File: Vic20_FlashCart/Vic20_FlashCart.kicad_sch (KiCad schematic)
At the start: 45 parts, among them U1 SST39LF040, U2 SST39LF040, U3 IS62C256AL, U4 7400, U5 74LS21

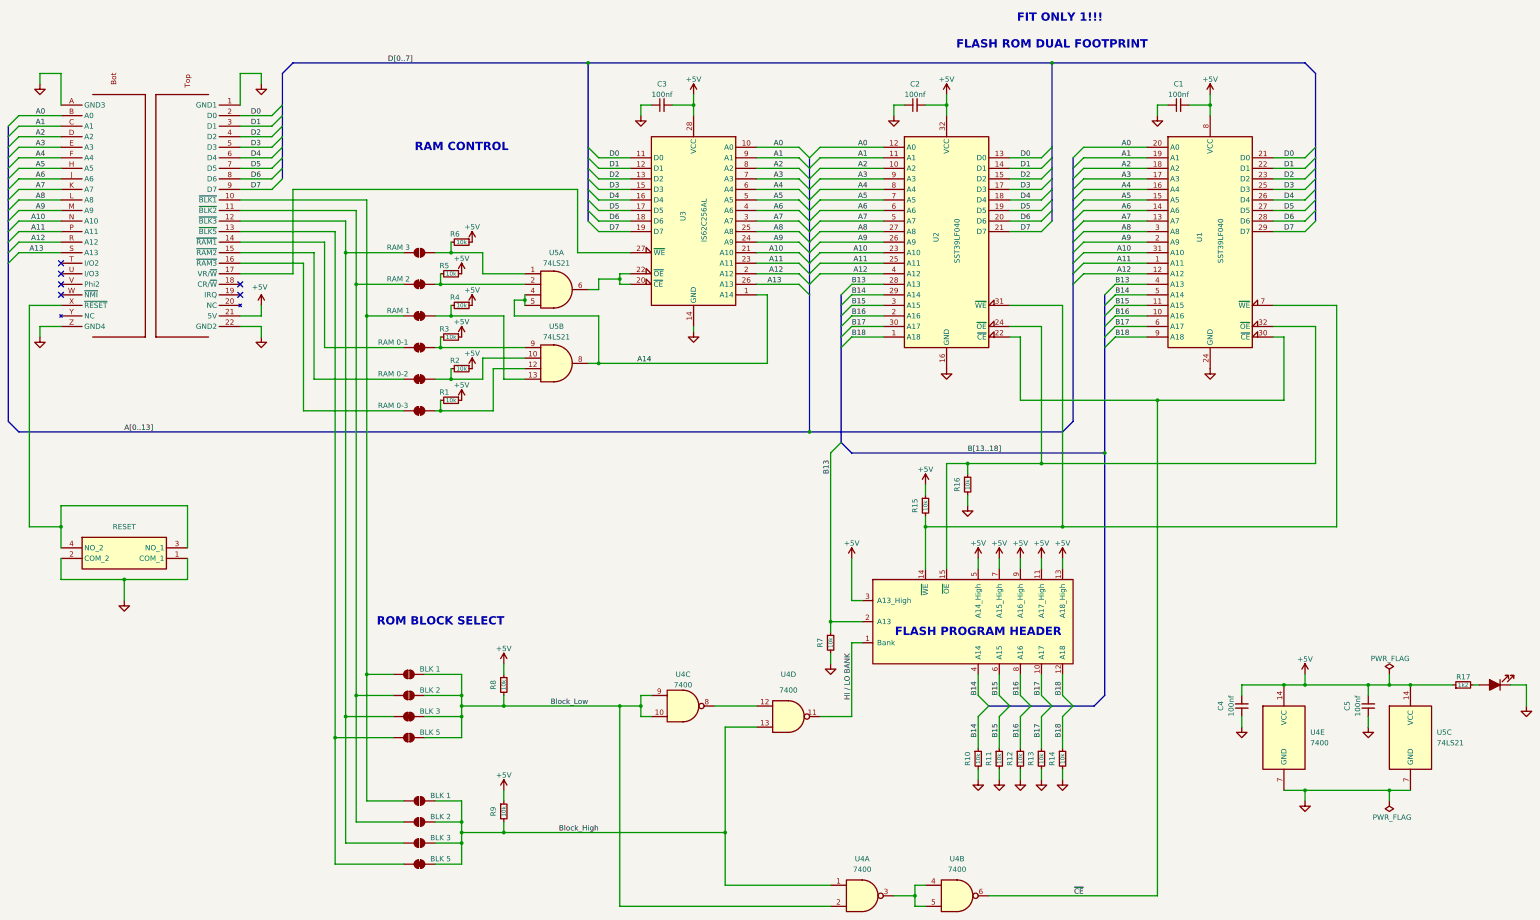
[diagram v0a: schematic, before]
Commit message: - Updated Vic20 Flash Cart files to Ki-CAD 9.x - Cleaned up some component names and generated ibom's
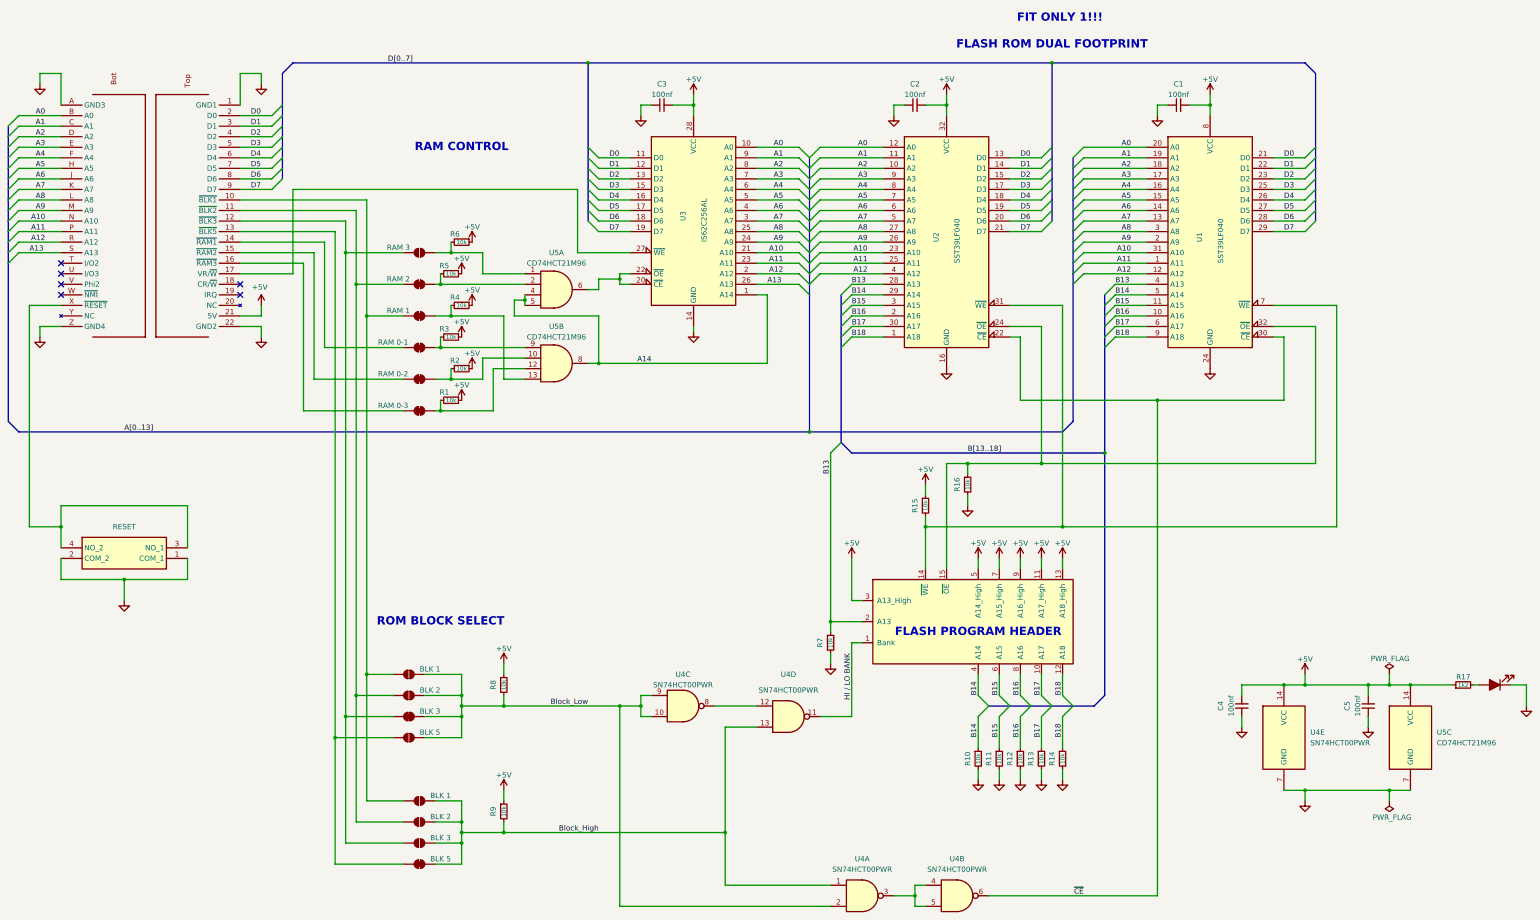
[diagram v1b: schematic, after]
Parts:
- J3: value ~ -> Pin Headers
- U4: value 7400 -> SN74HCT00PWR
- U5: value 74LS21 -> CD74HCT21M96
- X1: value ~ -> Cart Fingers
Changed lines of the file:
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@@
 			)
 		)
-		(property "Value" "7400"
+		(property "Value" "SN74HCT00PWR"
 			(at 213.3517 186.69 0)
 			(effects
@@
 			)
 		)
-		(property "Value" "74LS21"
+		(property "Value" "CD74HCT21M96"
 			(at 369.57 199.3899 0)
 			(effects
@@
 	)
 	(symbol
+		(lib_name "74LS21_2")
 		(lib_id "74xx:74LS21")
 		(at 157.48 107.95 0)
@@
 			)
 		)
-		(property "Value" "74LS21"
+		(property "Value" "CD74HCT21M96"
 			(at 157.4703 101.6 0)
 			(effects
@@
 			)
 		)
-		(property "Value" "~"
+		(property "Value" "Cart Fingers"
 			(at 88.9 78.74 90)
 			(effects
@@
 			)
 		)
-		(property "Value" "7400"
+		(property "Value" "SN74HCT00PWR"
 			(at 187.96 185.42 0)
 			(effects
@@
 	)
 	(symbol
+		(lib_name "74LS21_1")
 		(lib_id "74xx:74LS21")
 		(at 157.48 90.17 0)
@@
 			)
 		)
-		(property "Value" "74LS21"
+		(property "Value" "CD74HCT21M96"
 			(at 157.4703 83.82 0)
 			(effects
@@
 			)
 		)
-		(property "Value" "7400"
+		(property "Value" "SN74HCT00PWR"
 			(at 231.1317 229.87 0)
 			(effects
@@
 			)
 		)
-		(property "Value" "~"
+		(property "Value" "Pin Headers"
 			(at 262.89 176.53 0)
 			(effects
@@
 			)
 		)
-		(property "Value" "7400"
+		(property "Value" "SN74HCT00PWR"
 			(at 253.9917 229.87 0)
 			(effects
@@
 			)
 		)
-		(property "Value" "7400"
+		(property "Value" "SN74HCT00PWR"
 			(at 339.09 199.3899 0)
 			(effects
